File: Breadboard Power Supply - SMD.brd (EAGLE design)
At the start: 54.6 x 16.5 mm, 24 parts, among them J1 POWER_JACKTYLERALT1, U1 V_REG_317SMD

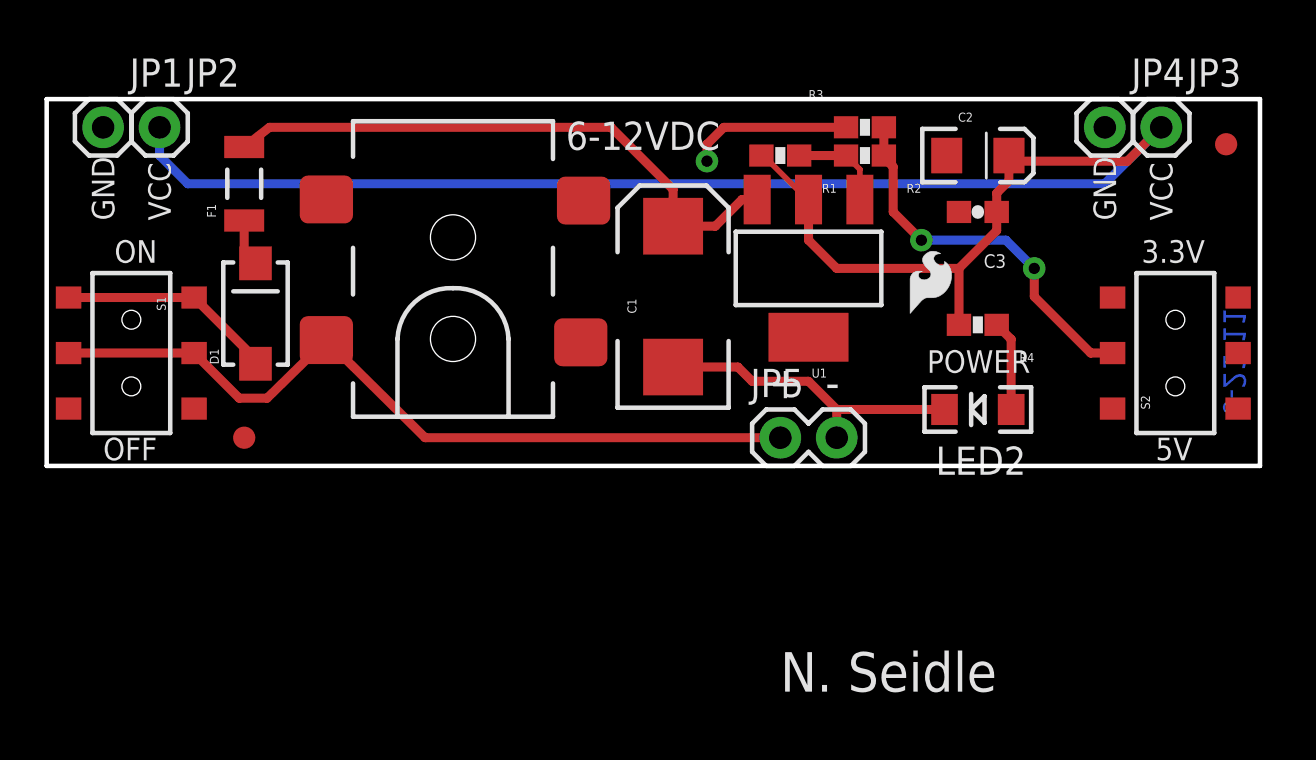
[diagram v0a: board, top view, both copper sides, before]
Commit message: Updated frame, rerouted traces, added OSHW
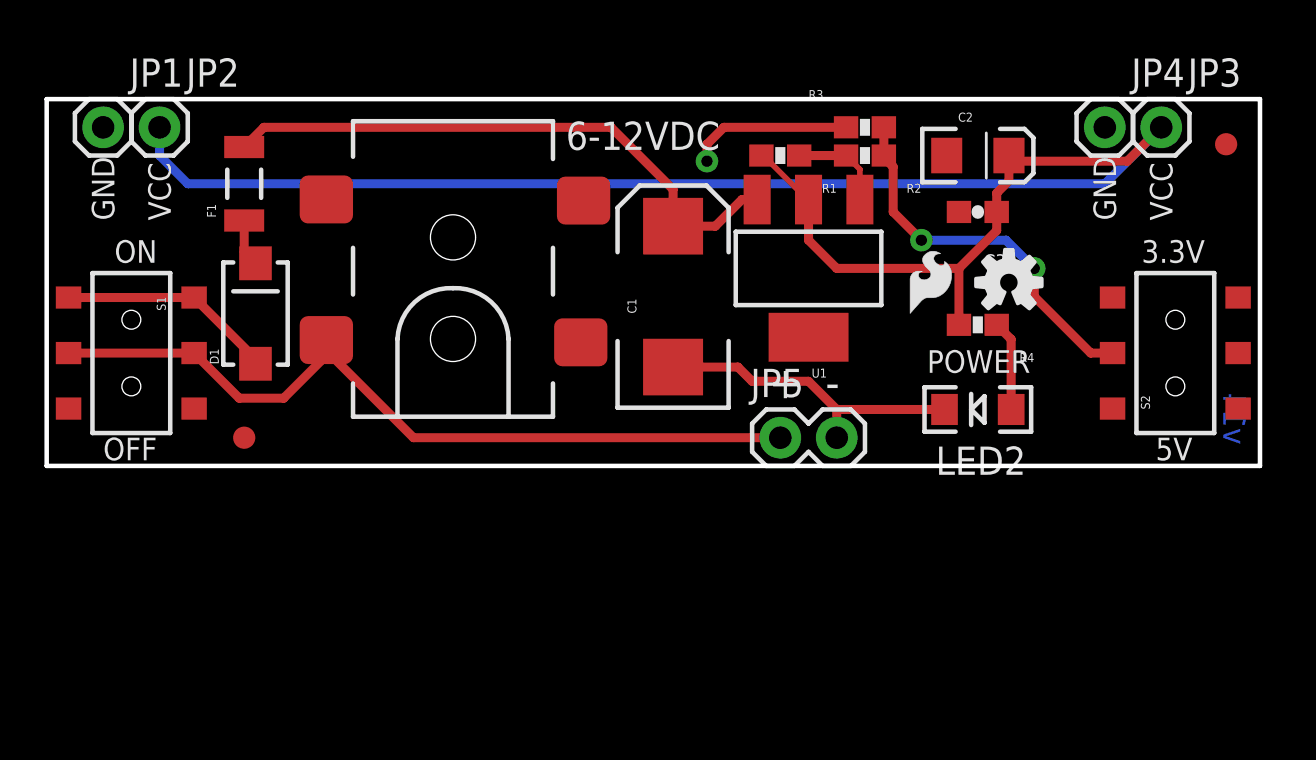
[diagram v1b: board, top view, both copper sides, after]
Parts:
- removed U$5: CREATIVE_COMMONS, SparkFun:CREATIVE_COMMONS
- added FRAME1: FRAME-LETTER, SparkFun-Aesthetics:CREATIVE_COMMONS
- added LOGO1: OSHW-LOGOS, SparkFun-Aesthetics:OSHW-LOGO-S
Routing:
- net VIN: track 36.6 -> 35.9 mm
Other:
- board text added: "Revised By: T Talmage"
- board text added: "v14"
- board text removed: "6-21-11"
